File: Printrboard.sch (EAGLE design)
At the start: 122 parts, among them J1 MICROSD, J3 ATX, Q1 RFP30N06LE, Q2 RFP30N06LE, Q3 RFP30N06LE, U1 LM2841, U2 A4982, U3 A4982, U4 A4982, U5 A4982, U6 AT90USB1286, U7 AP7313, U8 TXB0104, X1 16MHz, X2 USB-MICROB

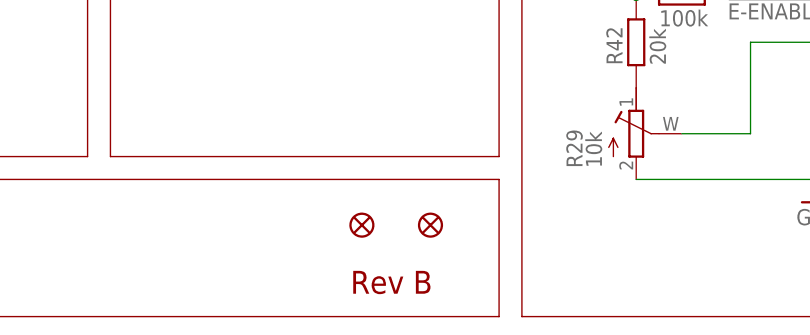
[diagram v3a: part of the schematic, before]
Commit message: Fixes for Rev C
-Made all mounting holes the same size
-Changed package for stepper solder jumpers to be connected by copper by
default
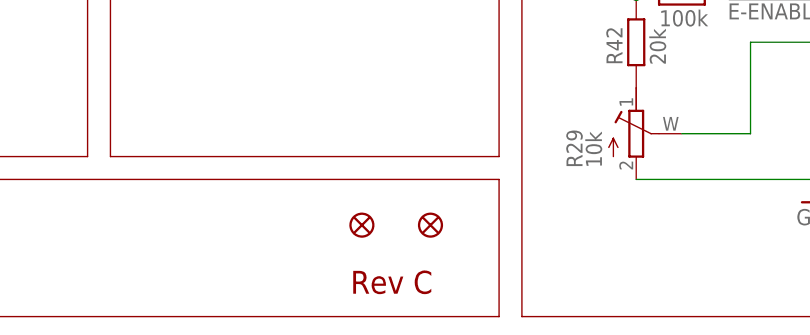
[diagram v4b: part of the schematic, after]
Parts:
- MS-E, MS-X, MS-Y, MS-Z: device printrbot:SOLDERJUMPER_2WAY -> printrbot:SOLDERJUMPER_2WAYCONNECTED
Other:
- note added: "Rev C"
- note removed: "Rev B"
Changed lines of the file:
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@@
 <grid distance="0.1" unitdist="inch" unit="inch" style="lines" multiple="1" display="no" altdistance="0.01" altunitdist="inch" altunit="inch"/>
 <layers>
-<layer number="1" name="Top" color="4" fill="1" visible="no" active="no"/>
-<layer number="2" name="Route2" color="1" fill="3" visible="no" active="no"/>
-<layer number="3" name="Route3" color="4" fill="3" visible="no" active="no"/>
-<layer number="4" name="Route4" color="1" fill="4" visible="no" active="no"/>
-<layer number="5" name="Route5" color="4" fill="4" visible="no" active="no"/>
-<layer number="6" name="Route6" color="1" fill="8" visible="no" active="no"/>
-<layer number="7" name="Route7" color="4" fill="8" visible="no" active="no"/>
-<layer number="8" name="Route8" color="1" fill="2" visible="no" active="no"/>
-<layer number="9" name="Route9" color="4" fill="2" visible="no" active="no"/>
-<layer number="10" name="Route10" color="1" fill="7" visible="no" active="no"/>
-<layer number="11" name="Route11" color="4" fill="7" visible="no" active="no"/>
-<layer number="12" name="Route12" color="1" fill="5" visible="no" active="no"/>
-<layer number="13" name="Route13" color="4" fill="5" visible="no" active="no"/>
-<layer number="14" name="Route14" color="1" fill="6" visible="no" active="no"/>
-<layer number="15" name="Route15" color="4" fill="6" visible="no" active="no"/>
-<layer number="16" name="Bottom" color="1" fill="1" visible="no" active="no"/>
-<layer number="17" name="Pads" color="2" fill="1" visible="no" active="no"/>
-<layer number="18" name="Vias" color="2" fill="1" visible="no" active="no"/>
-<layer number="19" name="Unrouted" color="6" fill="1" visible="no" active="no"/>
-<layer number="20" name="Dimension" color="15" fill="1" visible="no" active="no"/>
-<layer number="21" name="tPlace" color="7" fill="1" visible="no" active="no"/>
-<layer number="22" name="bPlace" color="7" fill="1" visible="no" active="no"/>
-<layer number="23" name="tOrigins" color="15" fill="1" visible="no" active="no"/>
-<layer number="24" name="bOrigins" color="15" fill="1" visible="no" active="no"/>
-<layer number="25" name="tNames" color="7" fill="1" visible="no" active="no"/>
-<layer number="26" name="bNames" color="7" fill="1" visible="no" active="no"/>
-<layer number="27" name="tValues" color="7" fill="1" visible="no" active="no"/>
-<layer number="28" name="bValues" color="7" fill="1" visible="no" active="no"/>
+<layer number="1" name="Top" color="4" fill="1" visible="yes" active="no"/>
+<layer number="2" name="Route2" color="16" fill="1" visible="yes" active="no"/>
+<layer number="3" name="Route3" color="17" fill="1" visible="yes" active="no"/>
+<layer number="4" name="Route4" color="1" fill="4" visible="yes" active="no"/>
+<layer number="5" name="Route5" color="4" fill="4" visible="yes" active="no"/>
+<layer number="6" name="Route6" color="1" fill="8" visible="yes" active="no"/>
+<layer number="7" name="Route7" color="4" fill="8" visible="yes" active="no"/>
+<layer number="8" name="Route8" color="1" fill="2" visible="yes" active="no"/>
+<layer number="9" name="Route9" color="4" fill="2" visible="yes" active="no"/>
+<layer number="10" name="Route10" color="1" fill="7" visible="yes" active="no"/>
+<layer number="11" name="Route11" color="4" fill="7" visible="yes" active="no"/>
+<layer number="12" name="Route12" color="1" fill="5" visible="yes" active="no"/>
+<layer number="13" name="Route13" color="4" fill="5" visible="yes" active="no"/>
+<layer number="14" name="Route14" color="1" fill="6" visible="yes" active="no"/>
+<layer number="15" name="Route15" color="4" fill="6" visible="yes" active="no"/>
+<layer number="16" name="Bottom" color="1" fill="1" visible="yes" active="no"/>
+<layer number="17" name="Pads" color="2" fill="1" visible="yes" active="no"/>
+<layer number="18" name="Vias" color="2" fill="1" visible="yes" active="no"/>
+<layer number="19" name="Unrouted" color="6" fill="1" visible="yes" active="no"/>
+<layer number="20" name="Dimension" color="15" fill="1" visible="yes" active="no"/>
+<layer number="21" name="tPlace" color="7" fill="1" visible="yes" active="no"/>
+<layer number="22" name="bPlace" color="7" fill="1" visible="yes" active="no"/>
+<layer number="23" name="tOrigins" color="15" fill="1" visible="yes" active="no"/>
+<layer number="24" name="bOrigins" color="15" fill="1" visible="yes" active="no"/>
+<layer number="25" name="tNames" color="7" fill="1" visible="yes" active="no"/>
+<layer number="26" name="bNames" color="7" fill="1" visible="yes" active="no"/>
+<layer number="27" name="tValues" color="7" fill="1" visible="yes" active="no"/>
+<layer number="28" name="bValues" color="7" fill="1" visible="yes" active="no"/>
 <layer number="29" name="tStop" color="7" fill="1" visible="no" active="no"/>
 <layer number="30" name="bStop" color="7" fill="1" visible="no" active="no"/>
@@
 <layer number="35" name="tGlue" color="7" fill="4" visible="no" active="no"/>
 <layer number="36" name="bGlue" color="7" fill="5" visible="no" active="no"/>
-<layer number="37" name="tTest" color="7" fill="1" visible="no" active="no"/>
-<layer number="38" name="bTest" color="7" fill="1" visible="no" active="no"/>
+<layer number="37" name="tTest" color="7" fill="1" visible="yes" active="no"/>
+<layer number="38" name="bTest" color="7" fill="1" visible="yes" active="no"/>
 <layer number="39" name="tKeepout" color="4" fill="11" visible="no" active="no"/>
 <layer number="40" name="bKeepout" color="1" fill="11" visible="no" active="no"/>
@@
 <layer number="44" name="Drills" color="7" fill="1" visible="no" active="no"/>
 <layer number="45" name="Holes" color="7" fill="1" visible="no" active="no"/>
-<layer number="46" name="Milling" color="3" fill="1" visible="no" active="no"/>
-<layer number="47" name="Measures" color="7" fill="1" visible="no" active="no"/>
-<layer number="48" name="Document" color="7" fill="1" visible="no" active="no"/>
-<layer number="49" name="Reference" color="7" fill="1" visible="no" active="no"/>
-<layer number="50" name="dxf" color="7" fill="1" visible="no" active="no"/>
-<layer number="51" name="tDocu" color="7" fill="1" visible="no" active="no"/>
-<layer number="52" name="bDocu" color="7" fill="1" visible="no" active="no"/>
-<layer number="53" name="tGND_GNDA" color="7" fill="9" visible="no" active="no"/>
-<layer number="54" name="bGND_GNDA" color="1" fill="9" visible="no" active="no"/>
-<layer number="56" name="wert" color="7" fill="1" visible="no" active="no"/>
+<layer number="46" name="Milling" color="3" fill="1" visible="yes" active="no"/>
+<layer number="47" name="Measures" color="7" fill="1" visible="yes" active="no"/>
+<layer number="48" name="Document" color="7" fill="1" visible="yes" active="no"/>
+<layer number="49" name="Reference" color="7" fill="1" visible="yes" active="no"/>
+<layer number="50" name="dxf" color="7" fill="1" visible="yes" active="no"/>
+<layer number="51" name="tDocu" color="7" fill="1" visible="yes" active="no"/>
+<layer number="52" name="bDocu" color="7" fill="1" visible="yes" active="no"/>
+<layer number="53" name="tGND_GNDA" color="7" fill="9" visible="yes" active="no"/>
+<layer number="54" name="bGND_GNDA" color="1" fill="9" visible="yes" active="no"/>
+<layer number="56" name="wert" color="7" fill="1" visible="yes" active="no"/>
 <layer number="91" name="Nets" color="2" fill="1" visible="yes" active="yes"/>
 <layer number="92" name="Busses" color="1" fill="1" visible="yes" active="yes"/>
@@
 <part name="GND46" library="SparkFun" deviceset="GND" device=""/>
 <part name="GND47" library="SparkFun" deviceset="GND" device=""/>
-<part name="MS-X" library="printrbot" deviceset="SOLDERJUMPER_2WAY" device=""/>
-<part name="MS-Y" library="printrbot" deviceset="SOLDERJUMPER_2WAY" device=""/>
-<part name="MS-Z" library="printrbot" deviceset="SOLDERJUMPER_2WAY" device=""/>
-<part name="MS-E" library="printrbot" deviceset="SOLDERJUMPER_2WAY" device=""/>
+<part name="MS-X" library="printrbot" deviceset="SOLDERJUMPER_2WAY" device="CONNECTED"/>
+<part name="MS-Y" library="printrbot" deviceset="SOLDERJUMPER_2WAY" device="CONNECTED"/>
+<part name="MS-Z" library="printrbot" deviceset="SOLDERJUMPER_2WAY" device="CONNECTED"/>
+<part name="MS-E" library="printrbot" deviceset="SOLDERJUMPER_2WAY" device="CONNECTED"/>
 <part name="R39" library="ipc-7351-resistor" deviceset="RESISTOR_" device="0805" value="20k"/>
 <part name="R40" library="ipc-7351-resistor" deviceset="RESISTOR_" device="0805" value="20k"/>
@@
 <text x="198.12" y="-7.62" size="1.778" layer="91" font="vector">Power Acc</text>
 <text x="6.35" y="-76.2" size="5.08" layer="94" ratio="10">Printrboard</text>
-<text x="222.25" y="-78.74" size="2.54" layer="94">Rev B</text>
+<text x="222.25" y="-78.74" size="2.54" layer="94">Rev C</text>
 <text x="101.6" y="-71.12" size="3.048" layer="94">Printrbot Electronics</text>
 <text x="64.77" y="-78.74" size="2.032" layer="94">Licensed under the Creative Commons Attributions ShareAlike 3.0 License</text>

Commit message: Board tweaks for rev D
Move endstop connectors apart for more clearance and move the labels for
the heaters around so they're easier to see
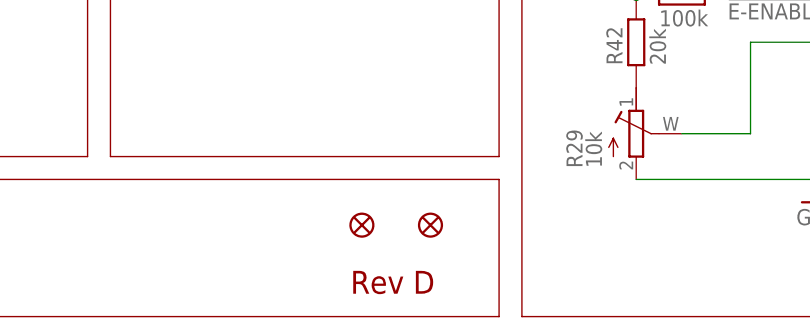
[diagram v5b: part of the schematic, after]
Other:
- note added: "Rev D"
- note removed: "Rev C"
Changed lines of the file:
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@@
 <grid distance="0.1" unitdist="inch" unit="inch" style="lines" multiple="1" display="no" altdistance="0.01" altunitdist="inch" altunit="inch"/>
 <layers>
-<layer number="1" name="Top" color="4" fill="1" visible="yes" active="no"/>
-<layer number="2" name="Route2" color="16" fill="1" visible="yes" active="no"/>
-<layer number="3" name="Route3" color="17" fill="1" visible="yes" active="no"/>
-<layer number="4" name="Route4" color="1" fill="4" visible="yes" active="no"/>
-<layer number="5" name="Route5" color="4" fill="4" visible="yes" active="no"/>
-<layer number="6" name="Route6" color="1" fill="8" visible="yes" active="no"/>
-<layer number="7" name="Route7" color="4" fill="8" visible="yes" active="no"/>
-<layer number="8" name="Route8" color="1" fill="2" visible="yes" active="no"/>
-<layer number="9" name="Route9" color="4" fill="2" visible="yes" active="no"/>
-<layer number="10" name="Route10" color="1" fill="7" visible="yes" active="no"/>
-<layer number="11" name="Route11" color="4" fill="7" visible="yes" active="no"/>
-<layer number="12" name="Route12" color="1" fill="5" visible="yes" active="no"/>
-<layer number="13" name="Route13" color="4" fill="5" visible="yes" active="no"/>
-<layer number="14" name="Route14" color="1" fill="6" visible="yes" active="no"/>
-<layer number="15" name="Route15" color="4" fill="6" visible="yes" active="no"/>
-<layer number="16" name="Bottom" color="1" fill="1" visible="yes" active="no"/>
-<layer number="17" name="Pads" color="2" fill="1" visible="yes" active="no"/>
-<layer number="18" name="Vias" color="2" fill="1" visible="yes" active="no"/>
-<layer number="19" name="Unrouted" color="6" fill="1" visible="yes" active="no"/>
-<layer number="20" name="Dimension" color="15" fill="1" visible="yes" active="no"/>
-<layer number="21" name="tPlace" color="7" fill="1" visible="yes" active="no"/>
-<layer number="22" name="bPlace" color="7" fill="1" visible="yes" active="no"/>
-<layer number="23" name="tOrigins" color="15" fill="1" visible="yes" active="no"/>
-<layer number="24" name="bOrigins" color="15" fill="1" visible="yes" active="no"/>
-<layer number="25" name="tNames" color="7" fill="1" visible="yes" active="no"/>
-<layer number="26" name="bNames" color="7" fill="1" visible="yes" active="no"/>
-<layer number="27" name="tValues" color="7" fill="1" visible="yes" active="no"/>
-<layer number="28" name="bValues" color="7" fill="1" visible="yes" active="no"/>
+<layer number="1" name="Top" color="4" fill="1" visible="no" active="no"/>
+<layer number="2" name="Route2" color="16" fill="1" visible="no" active="no"/>
+<layer number="3" name="Route3" color="17" fill="1" visible="no" active="no"/>
+<layer number="4" name="Route4" color="1" fill="4" visible="no" active="no"/>
+<layer number="5" name="Route5" color="4" fill="4" visible="no" active="no"/>
+<layer number="6" name="Route6" color="1" fill="8" visible="no" active="no"/>
+<layer number="7" name="Route7" color="4" fill="8" visible="no" active="no"/>
+<layer number="8" name="Route8" color="1" fill="2" visible="no" active="no"/>
+<layer number="9" name="Route9" color="4" fill="2" visible="no" active="no"/>
+<layer number="10" name="Route10" color="1" fill="7" visible="no" active="no"/>
+<layer number="11" name="Route11" color="4" fill="7" visible="no" active="no"/>
+<layer number="12" name="Route12" color="1" fill="5" visible="no" active="no"/>
+<layer number="13" name="Route13" color="4" fill="5" visible="no" active="no"/>
+<layer number="14" name="Route14" color="1" fill="6" visible="no" active="no"/>
+<layer number="15" name="Route15" color="4" fill="6" visible="no" active="no"/>
+<layer number="16" name="Bottom" color="1" fill="1" visible="no" active="no"/>
+<layer number="17" name="Pads" color="2" fill="1" visible="no" active="no"/>
+<layer number="18" name="Vias" color="2" fill="1" visible="no" active="no"/>
+<layer number="19" name="Unrouted" color="6" fill="1" visible="no" active="no"/>
+<layer number="20" name="Dimension" color="15" fill="1" visible="no" active="no"/>
+<layer number="21" name="tPlace" color="7" fill="1" visible="no" active="no"/>
+<layer number="22" name="bPlace" color="7" fill="1" visible="no" active="no"/>
+<layer number="23" name="tOrigins" color="15" fill="1" visible="no" active="no"/>
+<layer number="24" name="bOrigins" color="15" fill="1" visible="no" active="no"/>
+<layer number="25" name="tNames" color="7" fill="1" visible="no" active="no"/>
+<layer number="26" name="bNames" color="7" fill="1" visible="no" active="no"/>
+<layer number="27" name="tValues" color="7" fill="1" visible="no" active="no"/>
+<layer number="28" name="bValues" color="7" fill="1" visible="no" active="no"/>
 <layer number="29" name="tStop" color="7" fill="1" visible="no" active="no"/>
 <layer number="30" name="bStop" color="7" fill="1" visible="no" active="no"/>
@@
 <layer number="35" name="tGlue" color="7" fill="4" visible="no" active="no"/>
 <layer number="36" name="bGlue" color="7" fill="5" visible="no" active="no"/>
-<layer number="37" name="tTest" color="7" fill="1" visible="yes" active="no"/>
-<layer number="38" name="bTest" color="7" fill="1" visible="yes" active="no"/>
+<layer number="37" name="tTest" color="7" fill="1" visible="no" active="no"/>
+<layer number="38" name="bTest" color="7" fill="1" visible="no" active="no"/>
 <layer number="39" name="tKeepout" color="4" fill="11" visible="no" active="no"/>
 <layer number="40" name="bKeepout" color="1" fill="11" visible="no" active="no"/>
@@
 <layer number="44" name="Drills" color="7" fill="1" visible="no" active="no"/>
 <layer number="45" name="Holes" color="7" fill="1" visible="no" active="no"/>
-<layer number="46" name="Milling" color="3" fill="1" visible="yes" active="no"/>
-<layer number="47" name="Measures" color="7" fill="1" visible="yes" active="no"/>
-<layer number="48" name="Document" color="7" fill="1" visible="yes" active="no"/>
-<layer number="49" name="Reference" color="7" fill="1" visible="yes" active="no"/>
-<layer number="50" name="dxf" color="7" fill="1" visible="yes" active="no"/>
-<layer number="51" name="tDocu" color="7" fill="1" visible="yes" active="no"/>
-<layer number="52" name="bDocu" color="7" fill="1" visible="yes" active="no"/>
-<layer number="53" name="tGND_GNDA" color="7" fill="9" visible="yes" active="no"/>
-<layer number="54" name="bGND_GNDA" color="1" fill="9" visible="yes" active="no"/>
-<layer number="56" name="wert" color="7" fill="1" visible="yes" active="no"/>
+<layer number="46" name="Milling" color="3" fill="1" visible="no" active="no"/>
+<layer number="47" name="Measures" color="7" fill="1" visible="no" active="no"/>
+<layer number="48" name="Document" color="7" fill="1" visible="no" active="no"/>
+<layer number="49" name="Reference" color="7" fill="1" visible="no" active="no"/>
+<layer number="50" name="dxf" color="7" fill="1" visible="no" active="no"/>
+<layer number="51" name="tDocu" color="7" fill="1" visible="no" active="no"/>
+<layer number="52" name="bDocu" color="7" fill="1" visible="no" active="no"/>
+<layer number="53" name="tGND_GNDA" color="7" fill="9" visible="no" active="no"/>
+<layer number="54" name="bGND_GNDA" color="1" fill="9" visible="no" active="no"/>
+<layer number="56" name="wert" color="7" fill="1" visible="no" active="no"/>
 <layer number="91" name="Nets" color="2" fill="1" visible="yes" active="yes"/>
 <layer number="92" name="Busses" color="1" fill="1" visible="yes" active="yes"/>
@@
 <text x="198.12" y="-7.62" size="1.778" layer="91" font="vector">Power Acc</text>
 <text x="6.35" y="-76.2" size="5.08" layer="94" ratio="10">Printrboard</text>
-<text x="222.25" y="-78.74" size="2.54" layer="94">Rev C</text>
+<text x="222.25" y="-78.74" size="2.54" layer="94">Rev D</text>
 <text x="101.6" y="-71.12" size="3.048" layer="94">Printrbot Electronics</text>
 <text x="64.77" y="-78.74" size="2.032" layer="94">Licensed under the Creative Commons Attributions ShareAlike 3.0 License</text>
